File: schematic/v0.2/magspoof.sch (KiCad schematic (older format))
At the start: 23 parts, among them IC1 STM32F042G6U6, IC3 DRV8835DSSR, P1 USB_A, P2 Expansion Port, P3 CONN_01X02, P4 Program Port, SW1 SW_PUSH, SW2 SW_PUSH, U1 MCP73831-2-OT

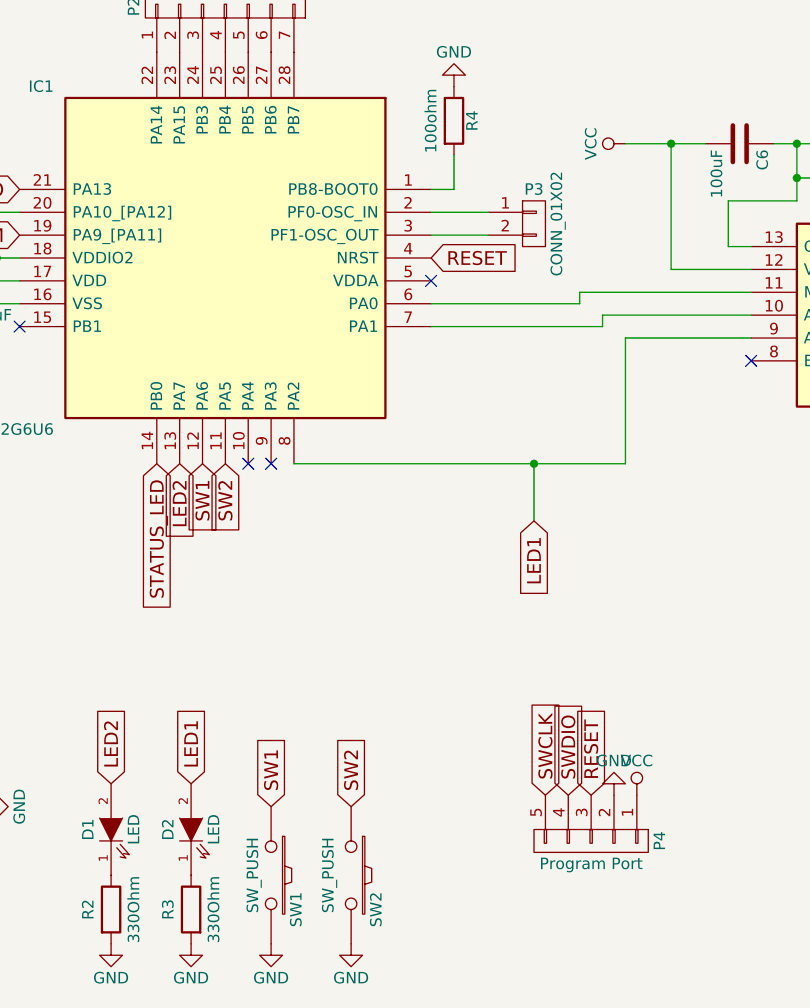
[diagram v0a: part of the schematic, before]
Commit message: Changed stm32 footprint
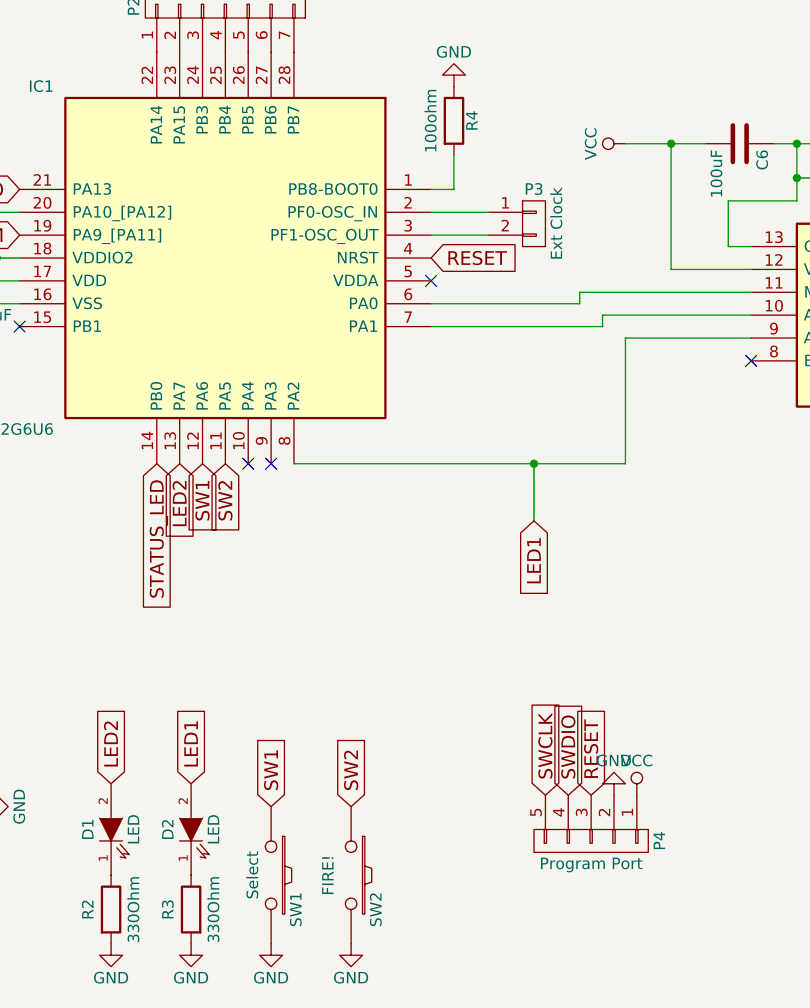
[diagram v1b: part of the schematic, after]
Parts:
- IC1: footprint Housings_DFN_QFN:QFN-24_4x4mm_Pitch0.5mm -> STM32F042G6U6:QFN50P400X400X60-28N
- P3: value CONN_01X02 -> Ext Clock
- SW1: value SW_PUSH -> Select
- SW2: value SW_PUSH -> FIRE!
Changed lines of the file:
@@
 P 5050 5900
 F 0 "SW1" H 5200 6010 50  0000 C CNN
-F 1 "SW_PUSH" H 5050 5820 50  0000 C CNN
+F 1 "Select" H 5050 5820 50  0000 C CNN
 F 2 "Switches:TACTILE_SWITCH_SMD_6.2MM_TALL" H 5050 5900 50  0001 C CNN
 F 3 "" H 5050 5900 50  0000 C CNN
@@
 F 0 "IC1" H 7400 3350 50  0000 L CNN
 F 1 "STM32F042G6U6" H 7400 1850 50  0000 L CNN
-F 2 "Housings_DFN_QFN:QFN-24_4x4mm_Pitch0.5mm" H 7400 1750 50  0001 L CNN
+F 2 "STM32F042G6U6:QFN50P400X400X60-28N" H 7400 1750 50  0001 L CNN
 F 3 "http://www.st.com/content/ccc/resource/technical/document/datasheet/52/ad/d0/80/e6/be/40/ad/DM00105814.pdf/files/DM00105814.pdf/jcr:content/translations/en.DM00105814.pdf" H 7400 1650 50  0001 L CNN
 F 4 "STMICROELECTRONICS - STM32F042G6U6 - MCU, 32BIT, CORTEX-M0, 48MHZ, UFQFN-28" H 7400 1550 50  0001 L CNN "Description"
@@
 P 5400 5900
 F 0 "SW2" H 5550 6010 50  0000 C CNN
-F 1 "SW_PUSH" H 5400 5800 50  0000 C CNN
+F 1 "FIRE!" H 5400 5800 50  0000 C CNN
 F 2 "Switches:TACTILE_SWITCH_SMD_6.2MM_TALL" H 5400 5900 50  0001 C CNN
 F 3 "" H 5400 5900 50  0000 C CNN
@@
 P 6200 3050
 F 0 "P3" H 6200 3200 50  0000 C CNN
-F 1 "CONN_01X02" V 6300 3050 50  0000 C CNN
+F 1 "Ext Clock" V 6300 3050 50  0000 C CNN
 F 2 "Pin_Headers:Pin_Header_Straight_1x02_Pitch2.54mm" H 6200 3050 50  0001 C CNN
 F 3 "" H 6200 3050 50  0000 C CNN
